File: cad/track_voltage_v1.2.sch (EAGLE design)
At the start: 37 parts, among them U2 74HC4051D, X1 1751248

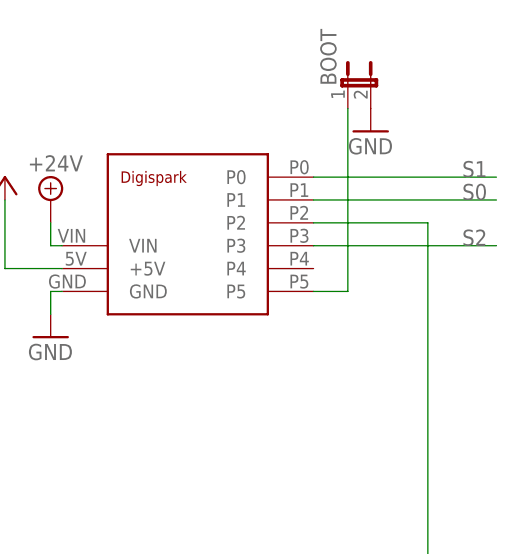
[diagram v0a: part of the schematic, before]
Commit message: Added some docs, updated code. Updated schematic to use PB5.
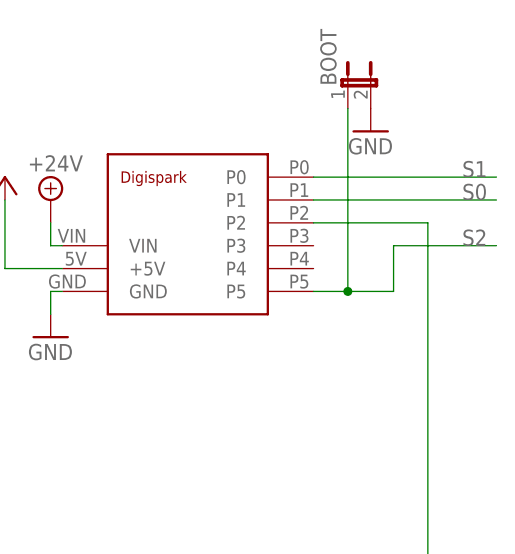
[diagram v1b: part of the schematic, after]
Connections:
- removed net N$1: BOOT.1, U$2.P5
- net S2: now also BOOT.1, U$2.P5; no longer U$2.P3
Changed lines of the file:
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@@
-</segment>
-</net>
-<net name="N$1" class="0">
-<segment>
-<pinref part="BOOT" gate="A" pin="1"/>
-<pinref part="U$2" gate="G$1" pin="P5"/>
-<wire x1="182.88" y1="142.24" x2="186.69" y2="142.24" width="0.1524" layer="91"/>
-<wire x1="186.69" y1="142.24" x2="186.69" y2="162.56" width="0.1524" layer="91"/>
 </segment>
 </net>
@@
 </segment>
 <segment>
-<pinref part="U$2" gate="G$1" pin="P3"/>
-<wire x1="182.88" y1="147.32" x2="203.2" y2="147.32" width="0.1524" layer="91"/>
 <label x="199.39" y="147.32" size="1.778" layer="95"/>
+<pinref part="BOOT" gate="A" pin="1"/>
+<pinref part="U$2" gate="G$1" pin="P5"/>
+<wire x1="191.77" y1="147.32" x2="203.2" y2="147.32" width="0.1524" layer="91"/>
+<wire x1="182.88" y1="142.24" x2="186.69" y2="142.24" width="0.1524" layer="91"/>
+<wire x1="186.69" y1="142.24" x2="186.69" y2="162.56" width="0.1524" layer="91"/>
+<wire x1="186.69" y1="142.24" x2="191.77" y2="142.24" width="0.1524" layer="91"/>
+<wire x1="191.77" y1="142.24" x2="191.77" y2="147.32" width="0.1524" layer="91"/>
+<junction x="186.69" y="142.24"/>
 </segment>
 </net>
